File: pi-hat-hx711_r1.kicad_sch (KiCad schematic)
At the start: 14 parts, among them J1 GPIO, J2 Conn_01x06, J5 Conn_01x06, Q1 S8550, U1 M24c64, U2 HX711, U3 TPS7A20xxxDQN

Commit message: loloxoxlxoxl
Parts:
- removed C1: 100n, symbol Device:C_Small
- added C1: 100nF, Capacitor_SMD:C_0603_1608Metric, symbol karl-marel-atomics:KC0603_100nF
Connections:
- net +3V3: now also C1.1
- net GND: now also C1.2
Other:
- note added: "TODO: add boost to ~6V block... (shared for all future boards) finish wiring up this fucker... set up pin connections! changes for other boards? => AA filters, => just the ananlog side then!"
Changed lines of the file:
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@@
+		)
+	)
+	(text "TODO:\nadd boost to ~6V block... (shared for all future boards)\nfinish wiring up this fucker...\nset up pin connections!\nchanges for other boards?\n=> AA filters,\n=> just the ananlog side then!\n"
+		(exclude_from_sim no)
+		(at 140.97 108.966 0)
+		(effects
+			(font
+				(size 1.27 1.27)
+			)
+			(justify left)
 		)
 	)
@@
 	(wire
 		(pts
+			(xy 67.31 165.1) (xy 67.31 175.26)
+		)
+		(stroke
+			(width 0)
+			(type solid)
+		)
+	)
+	(wire
+		(pts
 			(xy 76.2 33.02) (xy 73.66 33.02)
 		)
@@
 			(width 0)
 			(type default)
-		)
-	)
-	(wire
-		(pts
-			(xy 67.31 165.1) (xy 67.31 175.26)
-		)
-		(stroke
-			(width 0)
-			(type solid)
 		)
 	)
@@
 	)
 	(symbol
-		(lib_id "Device:C_Small")
+		(lib_id "karl-marel-atomics:KC0603_100nF")
 		(at 67.31 177.8 0)
 		(unit 1)
@@
 		(on_board yes)
 		(dnp no)
+		(fields_autoplaced yes)
 		(property "Reference" "C1"
-			(at 64.9858 176.6506 0)
-			(effects
-				(font
-					(size 1.27 1.27)
-				)
-				(justify right)
-			)
-		)
-		(property "Value" "100n"
-			(at 64.9858 178.9493 0)
-			(effects
-				(font
-					(size 1.27 1.27)
-				)
-				(justify right)
-			)
-		)
-		(property "Footprint" ""
-			(at 67.31 177.8 0)
+			(at 69.85 176.0271 0)
+			(effects
+				(font
+					(size 1.27 1.27)
+				)
+				(justify left)
+			)
+		)
+		(property "Value" "100nF"
+			(at 69.85 178.5671 0)
+			(effects
+				(font
+					(size 1.27 1.27)
+				)
+				(justify left)
+			)
+		)
+		(property "Footprint" "Capacitor_SMD:C_0603_1608Metric"
+			(at 66.802 181.61 0)
 			(effects
 				(font
@@
 			)
 		)
-		(property "Description" "Unpolarized capacitor, small symbol"
-			(at 67.31 177.8 0)
+		(property "Description" "50V, X7R"
+			(at 67.31 181.61 0)
 			(effects
 				(font
@@
 			)
 		)
-		(property "LCSC Part #" ""
-			(at 67.31 177.8 0)
+		(property "MPN" "CC0603KRX7R9BB104"
+			(at 67.056 181.61 0)
 			(effects
 				(font
@@
 			)
 		)
+		(property "LCSC Part #" "C14663"
+			(at 67.31 181.61 0)
+			(effects
+				(font
+					(size 1.27 1.27)
+				)
+				(hide yes)
+			)
+		)
+		(pin "2"
+		)
 		(pin "1"
 		)
-		(pin "2"
-		)
 		(instances
-			(project "RaspberryPi-HAT"
+			(project ""
 				(path "/e63e39d7-6ac0-4ffd-8aa3-1841a4541b55"
 					(reference "C1")

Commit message: lollll
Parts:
- added C3: 10uF, Capacitor_SMD:C_0805_2012Metric, symbol karl-marel-atomics:KC0805_10uF_25V
- added C4, C5: 100nF, Capacitor_SMD:C_0603_1608Metric, symbol karl-marel-atomics:KC0603_100nF
- added D1: SS14, Diode_SMD:D_SMA, symbol Diode:SS14
- added JP2: Jumper_2_Open, TestPoint:TestPoint_2Pads_Pitch2.54mm_Drill0.8mm, symbol Jumper:Jumper_2_Open
- added L1: 4u7H, Inductor_SMD:L_Sunlord_SWPA3015S, symbol Device:L_Small
- added R5: 100k, Resistor_SMD:R_0603_1608Metric, symbol karl-marel-atomics:KR0603_100k
- added R6: 360k, Resistor_SMD:R_0603_1608Metric, symbol karl-marel-atomics:KR0603_360k
- added U4: TPS61040DBV, Package_TO_SOT_SMD:SOT-23-5, symbol Regulator_Switching:TPS61040DBV
- C1, C2, R1, R2, R3, R4: jlcbasic (none) -> basic
- J2, U2, U3: jlcbasic (none) -> 0
- Q1, U1: jlcbasic (none) -> extplus
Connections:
- net +5V: now also U4.4 (EN), U4.5 (VIN)
- net +VDC: now also Q1.3 (C), U2.3 (AVDD), C3.1, C4.1
- net -VDC: now also U2.5 (AGND), C5.2
- net at U2.6 (VBG): now also C5.1
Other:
- note added: "Imagine trusting a linux SBC 5V supply... l0l"
- note added: "target out 5.9V tps7a20 is dropout at 140mV, so that's plenty."
- note added: "vout = 1.233*(1+r1/r2)"
- moved on the sheet: U3

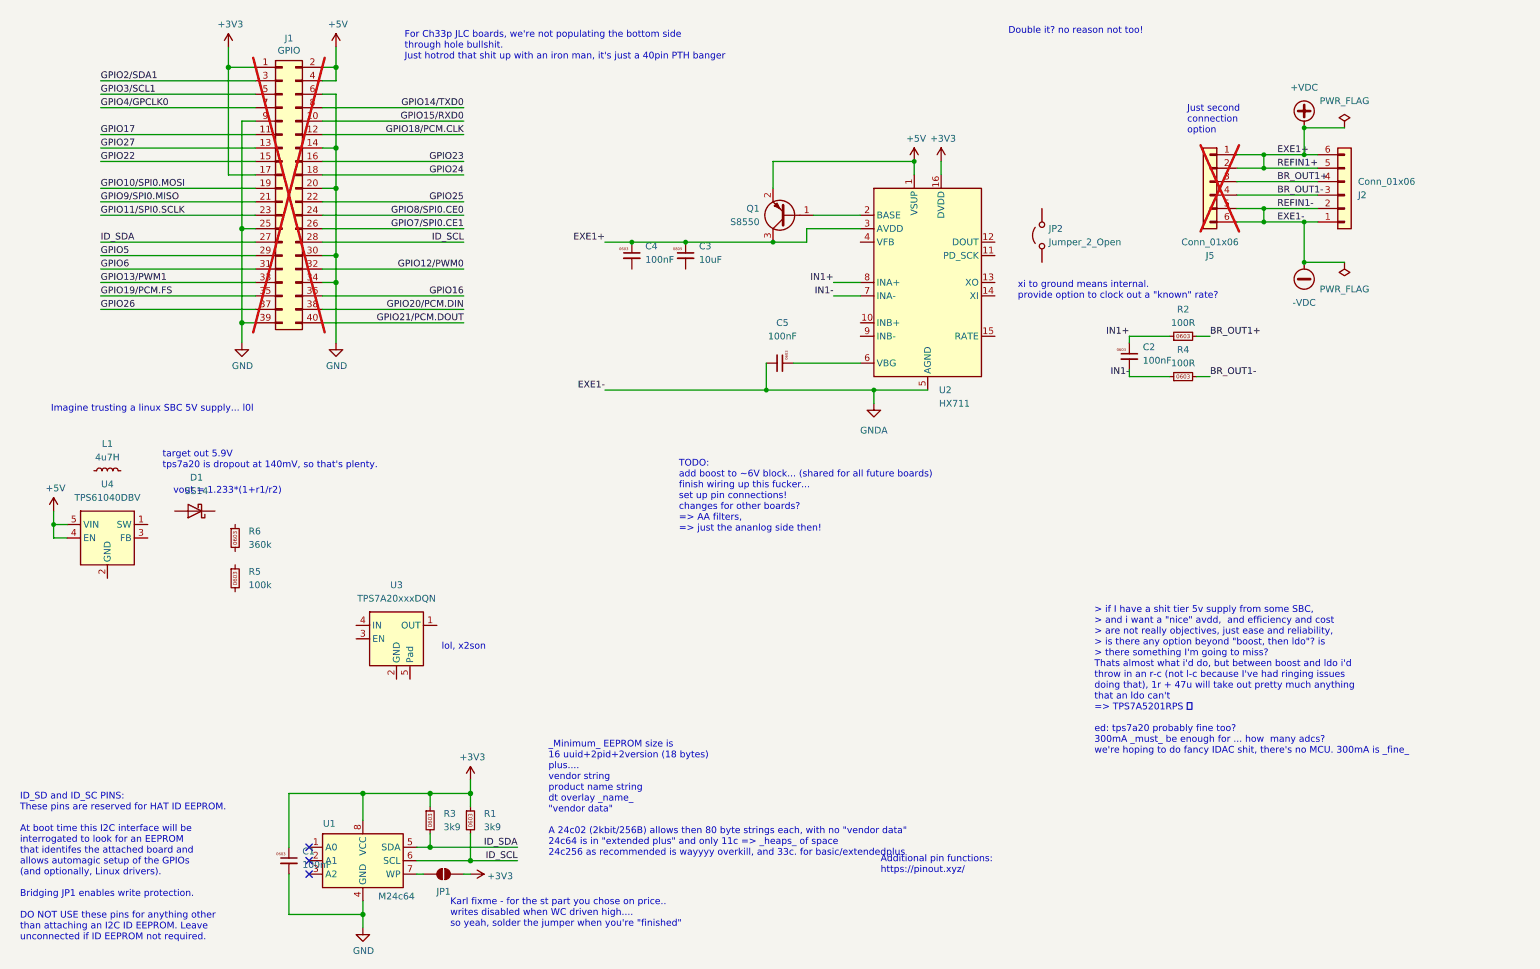
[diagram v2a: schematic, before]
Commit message: continuing.
might as well have channel b be usable for sense.
provide options for bypassing power shits though.
still ratiometric, just avoiding whatever is in the hx711 itself.
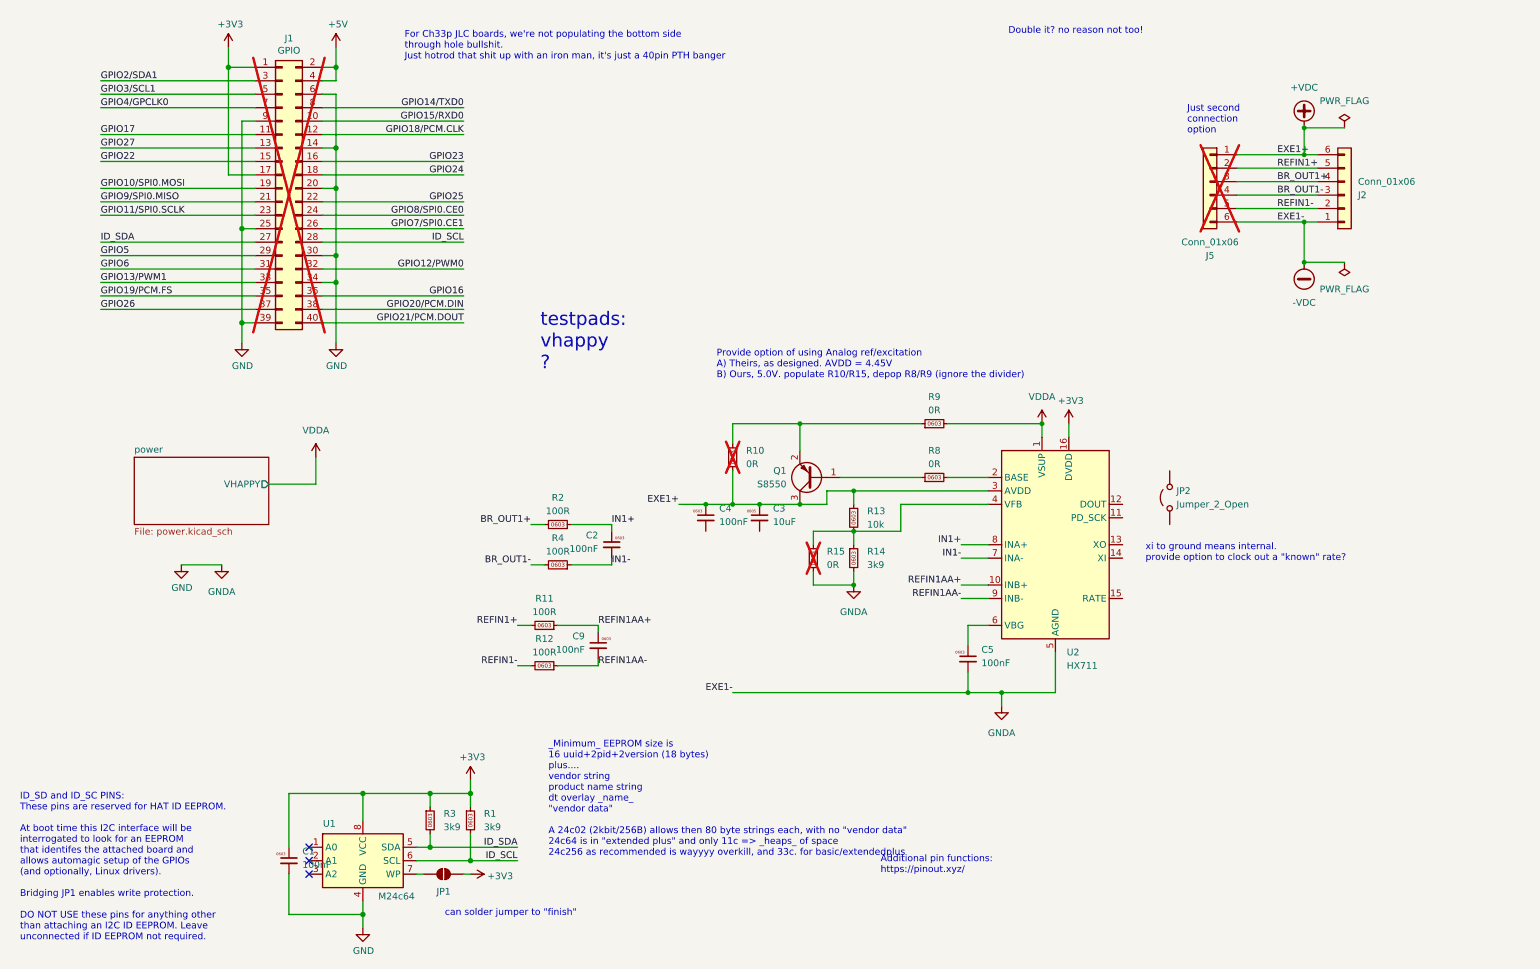
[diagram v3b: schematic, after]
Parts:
- removed D1: SS14, Diode_SMD:D_SMA, symbol Diode:SS14
- removed L1: 4u7H, Inductor_SMD:L_Sunlord_SWPA3015S, symbol Device:L_Small
- removed R5: 100k, Resistor_SMD:R_0603_1608Metric, symbol karl-marel-atomics:KR0603_100k
- removed R6: 360k, Resistor_SMD:R_0603_1608Metric, symbol karl-marel-atomics:KR0603_360k
- removed U3: TPS7A20xxxDQN, Package_SON:Texas_X2SON-4_1x1mm_P0.65mm, symbol Regulator_Linear:TPS7A20xxxDQN
- removed U4: TPS61040DBV, Package_TO_SOT_SMD:SOT-23-5, symbol Regulator_Switching:TPS61040DBV
- added C9: 100nF, Capacitor_SMD:C_0603_1608Metric, symbol karl-marel-atomics:KC0603_100nF
- added R10, R15, R8, R9: 0R, Resistor_SMD:R_0603_1608Metric, symbol karl-marel-atomics:KR0603_0R
- added R11, R12: 100R, Resistor_SMD:R_0603_1608Metric, symbol karl-marel-atomics:KR0603_100R
- added R13: 10k, Resistor_SMD:R_0603_1608Metric, symbol karl-marel-atomics:KR0603_10k
- added R14: 3k9, Resistor_SMD:R_0603_1608Metric, symbol karl-marel-atomics:KR0603_3k9
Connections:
- net GND is gone; now on net -VDC: C1.2, J1.14 (Pin_14), J1.20 (Pin_20), J1.25 (Pin_25), J1.30 (Pin_30), J1.34 (Pin_34), J1.39 (Pin_39), J1.6 (Pin_6), J1.9 (Pin_9), U1.4 (GND)
- net +5V: no longer Q1.2 (E), U2.1 (VSUP)
- net +VDC: now also R10.1, R13.1; no longer J2.5 (Pin_5), J5.2 (Pin_2)
- net -VDC: now also R14.2, R15.1; no longer J2.2 (Pin_2), J5.5 (Pin_5)
- net at Q1.1 (B): now also R8.1; no longer U2.2 (BASE)
- net REFIN1AA+: now reaches U2.10 (INB+)
- net REFIN1AA+: now also C9.1, R11.1
- net at U2.4 (VFB): now also R13.2, R14.1, R15.2
- net REFIN1AA-: now reaches U2.9 (INB-)
- net REFIN1AA-: now also C9.2, R12.1
- new net: Q1.2 (E), R10.2, R9.1
- new net: R8.2, U2.2 (BASE)
- new net REFIN1+: J2.5 (Pin_5), J5.2 (Pin_2), R11.2
- new net REFIN1-: J2.2 (Pin_2), J5.5 (Pin_5), R12.2
- new net VDDA: R9.2, U2.1 (VSUP)
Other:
- added sheet power (power.kicad_sch)
- note added: "Provide option of using Analog ref/excitation A) Theirs, as designed. AVDD = 4.45V B) Ours, 5.0V. populate R10/R15, depop R8/R9 (ignore the divider)"
- note added: "can solder jumper to "finish""
- note added: "testpads: vhappy ?"
- note removed: "> if I have a shit tier 5v supply from some SBC, > and i want a "nice" avdd, and efficiency and cost > are not really objectives, just ease and reliability, > is there any option beyond "boost, then ldo"? is > there something I'm going to miss? Thats almost what i'd do, but between boost and ldo i'd throw in an r-c (not l-c because I've had ringing issues doing that), 1r + 47u will take out prett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"
- note removed: "Imagine trusting a linux SBC 5V supply... l0l"
- note removed: "Karl fixme - for the st part you chose on price.. writes disabled when WC driven high.... so yeah, solder the jumper when you're "finished""
- note removed: "TODO: add boost to ~6V block... (shared for all future boards) finish wiring up this fucker... set up pin connections! changes for other boards? => AA filters, => just the ananlog side then!"
- note removed: "lol, x2son"
- note removed: "target out 5.9V tps7a20 is dropout at 140mV, so that's plenty."
- note removed: "vout = 1.233*(1+r1/r2)"
- moved on the sheet: C2, C3, C4, C5, JP2, Q1, R2, R4, U2

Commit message: add the sheets that we refactored too...
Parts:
- removed C2, C4, C5, C9: 100nF, Capacitor_SMD:C_0603_1608Metric, symbol karl-marel-atomics:KC0603_100nF
- removed C3: 10uF, Capacitor_SMD:C_0805_2012Metric, symbol karl-marel-atomics:KC0805_10uF_25V
- removed JP2: Jumper_2_Open, TestPoint:TestPoint_2Pads_Pitch2.54mm_Drill0.8mm, symbol Jumper:Jumper_2_Open
- removed Q1: S8550, Package_TO_SOT_SMD:SOT-23, symbol Transistor_BJT:BC858
- removed R10, R15, R8, R9: 0R, Resistor_SMD:R_0603_1608Metric, symbol karl-marel-atomics:KR0603_0R
- removed R11, R12, R2, R4: 100R, Resistor_SMD:R_0603_1608Metric, symbol karl-marel-atomics:KR0603_100R
- removed R13: 10k, Resistor_SMD:R_0603_1608Metric, symbol karl-marel-atomics:KR0603_10k
- removed R14: 3k9, Resistor_SMD:R_0603_1608Metric, symbol karl-marel-atomics:KR0603_3k9
- removed U2: HX711, Package_SO:SOIC-16_3.9x9.9mm_P1.27mm, symbol Analog_ADC:HX711
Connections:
- net -VDC: no longer C1.2, J1.14 (Pin_14), J1.20 (Pin_20), J1.25 (Pin_25), J1.30 (Pin_30), J1.34 (Pin_34), J1.39 (Pin_39), J1.6 (Pin_6), J1.9 (Pin_9), U1.4 (GND)
- new net GND: C1.2, J1.14 (Pin_14), J1.20 (Pin_20), J1.25 (Pin_25), J1.30 (Pin_30), J1.34 (Pin_34), J1.39 (Pin_39), J1.6 (Pin_6), J1.9 (Pin_9), U1.4 (GND)
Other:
- added sheet Analog (analog.kicad_sch)
- sheet power ports: added VNOISY; removed none
- note added: "$JOB order 6 pin load cell connectors"
- note added: "Imagine trusting a linux SBC 5V supply... l0l"
- note removed: "Double it? no reason not too!"
- note removed: "Provide option of using Analog ref/excitation A) Theirs, as designed. AVDD = 4.45V B) Ours, 5.0V. populate R10/R15, depop R8/R9 (ignore the divider)"
- note removed: "can solder jumper to "finish""
- note removed: "testpads: vhappy ?"
- note removed: "xi to ground means internal. provide option to clock out a "known" rate?"
- moved on the sheet: J2, J5

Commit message: rough blocking out the pcb
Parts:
- JP1: footprint (none) -> Jumper:SolderJumper-2_P1.3mm_Open_TrianglePad1.0x1.5mm
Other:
- sheet Analog ports: added DCLK, DOUT, D_RATE, EXT_CLK_IN; removed none
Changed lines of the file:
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@@
+	(wire
+		(pts
+			(xy 127 99.06) (xy 139.7 99.06)
+		)
+		(stroke
+			(width 0)
+			(type default)
+		)
+	)
 	(wire
 		(pts
@@
 	(wire
 		(pts
+			(xy 127 96.52) (xy 139.7 96.52)
+		)
+		(stroke
+			(width 0)
+			(type default)
+		)
+	)
+	(wire
+		(pts
 			(xy 31.75 45.72) (xy 60.96 45.72)
 		)
@@
 	(wire
 		(pts
+			(xy 127 101.6) (xy 139.7 101.6)
+		)
+		(stroke
+			(width 0)
+			(type default)
+		)
+	)
+	(wire
+		(pts
 			(xy 185.42 93.98) (xy 177.8 93.98)
+		)
+		(stroke
+			(width 0)
+			(type default)
+		)
+	)
+	(wire
+		(pts
+			(xy 127 93.98) (xy 139.7 93.98)
 		)
 		(stroke
@@
 		)
 	)
+	(label "GPIO11{slash}SPI0.SCLK"
+		(at 127 93.98 180)
+		(effects
+			(font
+				(size 1.27 1.27)
+			)
+			(justify right bottom)
+		)
+	)
 	(label "GPIO19{slash}PCM.FS"
 		(at 31.75 71.12 0)
@@
 		)
 	)
+	(label "GPIO9{slash}SPI0.MISO"
+		(at 127 96.52 180)
+		(effects
+			(font
+				(size 1.27 1.27)
+			)
+			(justify right bottom)
+		)
+	)
 	(label "GPIO4{slash}GPCLK0"
 		(at 31.75 35.56 0)
@@
 		)
 	)
+	(label "GPIO8{slash}SPI0.CE0"
+		(at 127 99.06 180)
+		(effects
+			(font
+				(size 1.27 1.27)
+			)
+			(justify right bottom)
+		)
+	)
 	(label "REFIN1-"
 		(at 236.22 104.14 0)
@@
 			)
 			(justify left bottom)
+		)
+	)
+	(label "GPIO13{slash}PWM1"
+		(at 127 101.6 180)
+		(effects
+			(font
+				(size 1.27 1.27)
+			)
+			(justify right bottom)
 		)
 	)
@@
 			)
 		)
-		(property "Footprint" ""
+		(property "Footprint" "Jumper:SolderJumper-2_P1.3mm_Open_TrianglePad1.0x1.5mm"
 			(at 96.52 180.34 0)
 			(effects
@@
 			)
 		)
+		(pin "DCLK" input
+			(at 139.7 93.98 180)
+			(effects
+				(font
+					(size 1.27 1.27)
+				)
+				(justify left)
+			)
+		)
+		(pin "DOUT" output
+			(at 139.7 96.52 180)
+			(effects
+				(font
+					(size 1.27 1.27)
+				)
+				(justify left)
+			)
+		)
+		(pin "D_RATE" input
+			(at 139.7 99.06 180)
+			(effects
+				(font
+					(size 1.27 1.27)
+				)
+				(justify left)
+			)
+		)
+		(pin "EXT_CLK_IN" input
+			(at 139.7 101.6 180)
+			(effects
+				(font
+					(size 1.27 1.27)
+				)
+				(justify left)
+			)
+		)
